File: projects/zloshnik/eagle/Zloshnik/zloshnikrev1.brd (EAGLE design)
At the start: 100 x 80 mm, 56 parts, among them IC2 78L05F, IC7 MEGA8-AI, Q1 IRLML2502, Q2 IRLML2502, Q3 IRLML2502, SW1 BUTTON-IT_1181

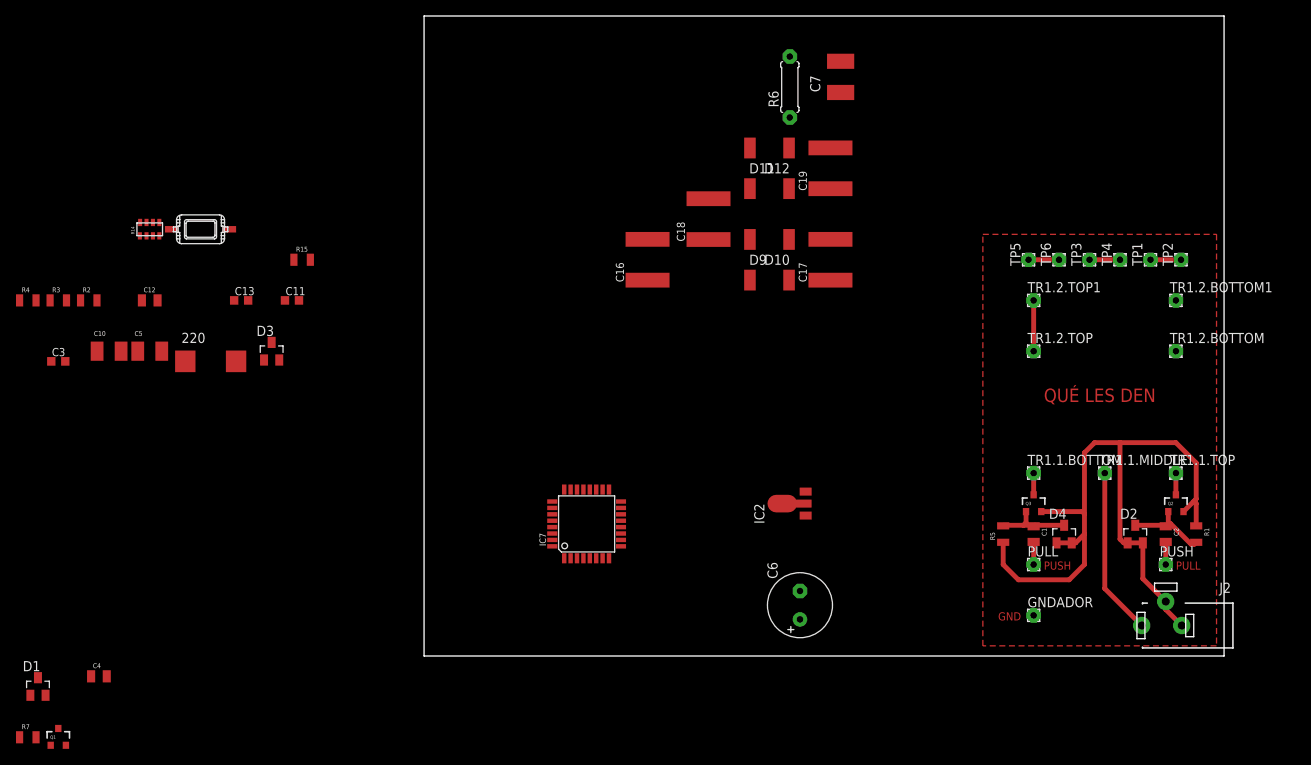
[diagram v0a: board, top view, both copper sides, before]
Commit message: read_dsn.py only pads no rotation
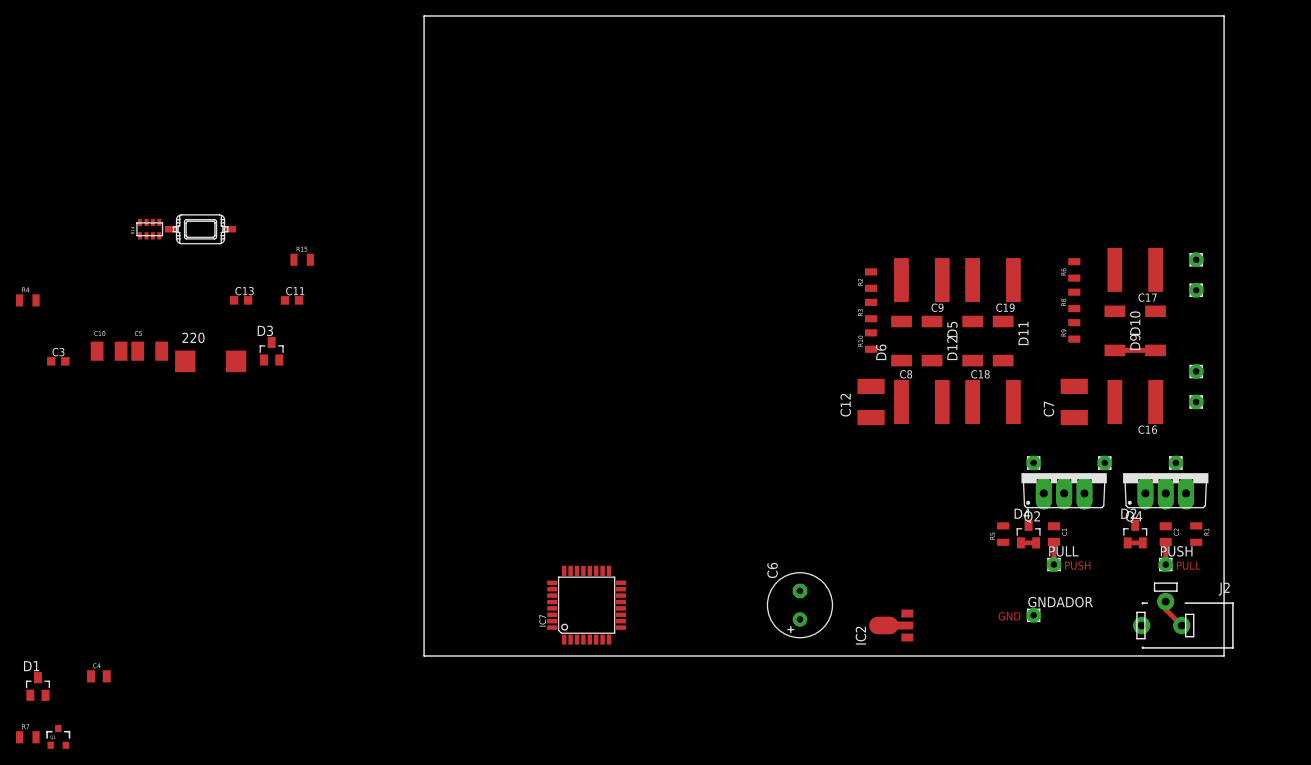
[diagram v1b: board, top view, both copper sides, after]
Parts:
- removed Q3: IRLML2502, xmaker:SOT23-3
- removed TP1, TP2, TP3, TP4, TP5, TP6: (no value), wirepad:1,6/0,8
- added C8, C9: 0,01 1kV, 0-rcl:C2220K
- added D5, D6: (no value), semicon-smd-ipc:SOD87
- added Q4: IRF630N, transistor-power:TO220BV
- added R10, R8, R9: 33K, rcl:R0805-SVO
- C12: value 1.0 -> 0,01 2kV; device rcl:C0805S -> 0-rcl:C1812
- C7: value 0,01 1kV -> 0,01 2kV
- Q2: value IRLML2502 -> IRF630N; device xmaker:SOT23-3 -> transistor-power:TO220BV
- R2: value 470K -> 33K
- R3: value 4K7 -> 33K
- R6: value 100k -> 33K; device 0-rcl:0207/7 -> rcl:R0805-SVO
- moved R3 101.6 mm to (55.9, 43.2), turned to 90 degrees
- moved R2 97.8 mm to (55.9, 47.0), turned to 90 degrees
- moved C12 91.1 mm to (55.9, 31.8), turned to 90 degrees
- moved C16 63.5 mm to (88.9, 31.8), turned to 180 degrees
- moved C7 50.0 mm to (81.3, 31.8)
- moved D9 48.7 mm to (91.4, 40.6), turned to 90 degrees
- moved D10 44.7 mm to (86.4, 40.6), turned to 270 degrees
- moved R6 42.3 mm to (81.3, 48.3)
- moved C18 42.3 mm to (71.1, 31.8), turned to 0 degrees
- moved C17 38.1 mm to (88.9, 48.3), turned to 180 degrees
- moved D12 35.0 mm to (68.6, 39.4), turned to 90 degrees
- moved D11 34.9 mm to (72.4, 39.4), turned to 270 degrees
- moved C19 24.7 mm to (71.1, 47.0), turned to 180 degrees
- moved TR1.2.TOP1 22.2 mm to (96.5, 35.6), turned to 90 degrees
- moved TR1.2.TOP 21.3 mm to (96.5, 31.8), turned to 90 degrees
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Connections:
- removed net +1KV: C7.2, R6.2
- removed net HV+: R2.1
- removed net N$8: TP3.1, TP4.1
- new net +300V: C7.2, R9.1
- new net -600V: C12.2, R10.1
- new net N$11: R6.1, R8.2
- new net N$14: C8.1, D5.2, D6.1
- new net N$17: C19.2, C9.1, D12.2, D5.1
- new net N$18: R10.2, R3.1
- net +5V: no longer D3.2
- net FBACK: no longer C12.1, D3.3, R2.2, R3.2
- net GND: now also C12.1, C19.1, D11.1, Q2.S, Q4.S; no longer C12.2, D3.1, Q2.2, Q3.2, R3.1
- net N$1: now also Q2.G; no longer Q3.1
- net N$12: now also R2.1, R3.2; no longer C18.2, D11.1, D12.2
- net N$13: now also R6.2; no longer C19.1, D11.2
- net N$15: now also C9.2, D6.2, R2.2; no longer C19.2, D12.1, R6.1
- net N$16: now also C18.2
- net N$2: now also Q4.D; no longer Q2.3
- net N$3: now also Q4.G; no longer Q2.1
- net N$4: now also Q2.D; no longer Q3.3
- net N$6: no longer C18.1
- net N$7: now also C18.1, C8.2, D11.2, D12.1; no longer TP1.1, TP2.1
- net N$9: now also R8.1, R9.2; no longer TP5.1, TP6.1
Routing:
- net GND: track 90.9 -> 7.63 mm
- net +UB: track 21.0 -> 0.00 mm
- net N$3: track 10.5 -> 0.00 mm
- net N$1: track 9.74 -> 0.17 mm
- net N$16: track 6.35 -> 0.00 mm
- net N$6: track 0.00 -> 5.09 mm
- net N$9: track 3.81 -> 0.00 mm
- net N$8: track 3.81 -> 0.00 mm
- net N$7: track 3.81 -> 0.00 mm
- net N$4: track 2.71 -> 0.00 mm
- net N$2: track 2.71 -> 0.00 mm
- removed copper zone on layer 1, net GND
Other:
- board text removed: "QUÉ LES DEN"
